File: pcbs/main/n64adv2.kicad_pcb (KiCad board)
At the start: 4 copper layers, 80 x 89.8 mm, 158 parts, among them Q1 2N2222, Q2 2N2222, Q3 2N2222, U1 10M16SAE144/10M25SAE144, U10 TLV70225DBV, U11 TLV70025DDC, U12 TLV70218DBV, U13 TLV70033DDC, U2 ADV7513, U3 AS4C8M16SA-xTCN, U4 SI5356A-B-GMR, U5 ECS-3225MV-500-CN-TR, U6 ECS-3225MVLC-245.7-CN-TR, X1 3-1734592-0, X2 3020-10-0300-00, X3 2000-1-2-41-00-BK, X4 TEI0005, X5 USB3140-30-0170-0-C, Y41 445I23D27M00000

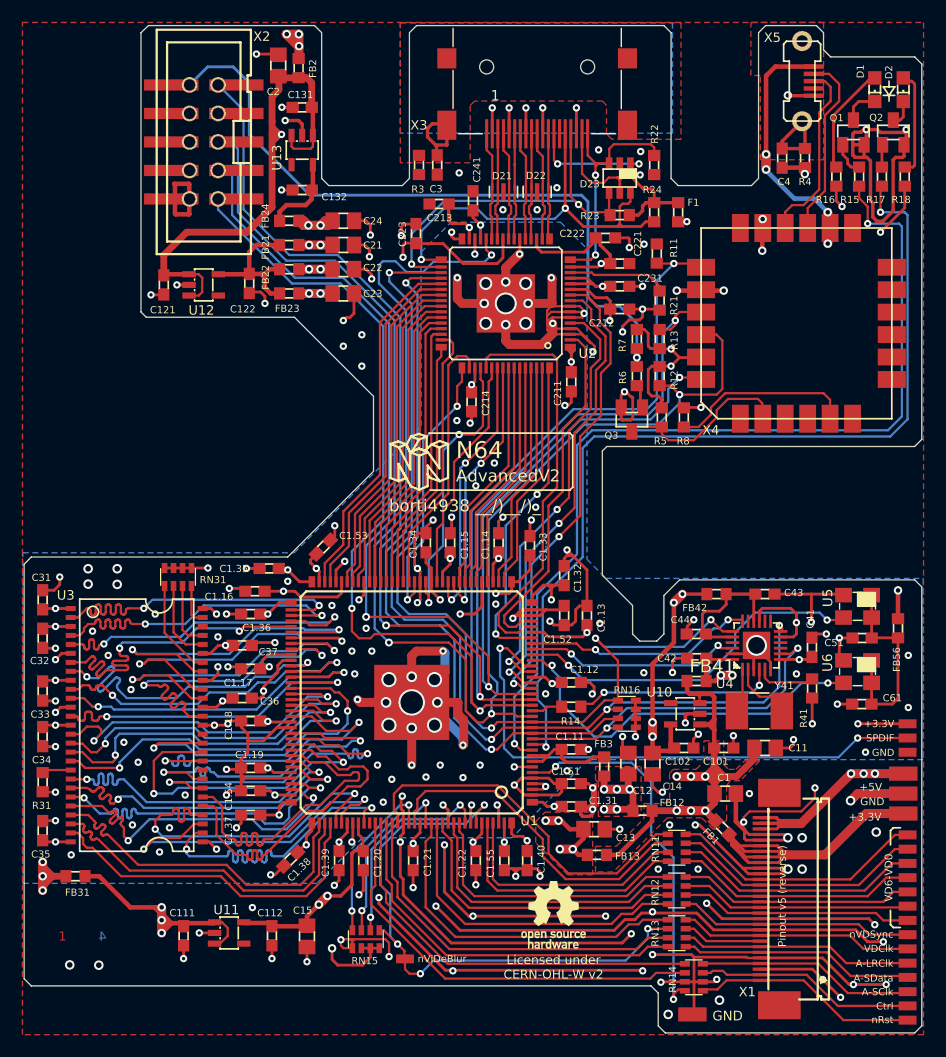
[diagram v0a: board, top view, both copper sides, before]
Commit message: Update main-PCB: - fixing solder mask - slightly move components a bit (USB port, JTAG, C2, ...)
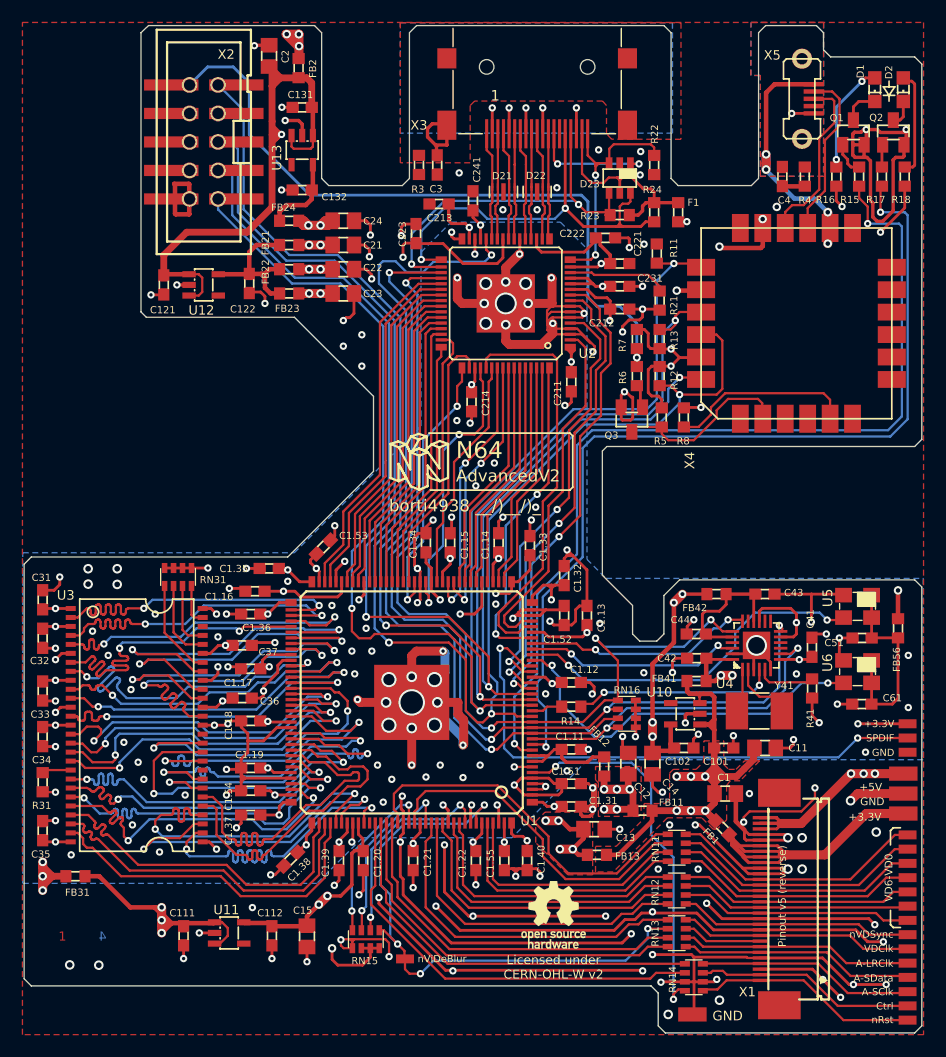
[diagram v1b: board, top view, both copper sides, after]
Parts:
- X4: value TEI0005 -> >VALUE
- moved R4 1.65 mm to (178.1, 73.6)
- moved C4 1.64 mm to (176.1, 73.6)
- moved X5 1.57 mm to (177.8, 66.7)
- moved C2 1.18 mm to (130.3, 62.9)
- renumbered FB12 to FB11, FB3 to FB12
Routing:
- net Net-(C4-Pad2): track 18.4 -> 0.00 mm
- net GND: track 607.0 -> 616.0 mm, vias 229 -> 228
- net VCCIO_3V3: track 338.5 -> 334.8 mm
- net +5V: track 91.0 -> 94.0 mm
- net Net-(X4-Pad14): track 30.7 -> 29.1 mm
- net Net-(X4-Pad15): track 16.6 -> 15.3 mm
- net Net-(X4-Pad16): track 16.6 -> 15.6 mm
- net Net-(D1-PadA): track 9.78 -> 9.86 mm, vias 0 -> 2
- added copper zone on B.Cu, net Net-(C4-Pad2)
- added copper zone on In2.Cu, net Net-(C4-Pad2)
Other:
- board text added: "N64Adv2_20231119"
- board text removed: "N64Adv2_20231105"
